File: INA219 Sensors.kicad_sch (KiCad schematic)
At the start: 20 parts, among them J5 Conn_01x06, U2 INA219AxD, U3 INA219AxD, U4 LTV-817, U5 LTV-817, U7 ESP32-C3 Pro Mini, U8 AMS1117-3.3

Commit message: DRC check
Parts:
- J5: value Conn_01x06 -> Esternal; footprint Connector_JST:JST_PH_S6B-PH-K_1x06_P2.00mm_Horizontal -> Connector_JST:JST_PH_B8B-PH-K_1x08_P2.00mm_Vertical; symbol Connector_Generic:Conn_01x06 -> Connector_Generic:Conn_01x08
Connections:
- net GNDPWR: no longer U8.4 (GND2)
- net at U7.0 (GPIO0/A0): now also J5.8 (Pin_8)
- net at U7.1 (GPIO1/A1): now also J5.7 (Pin_7)

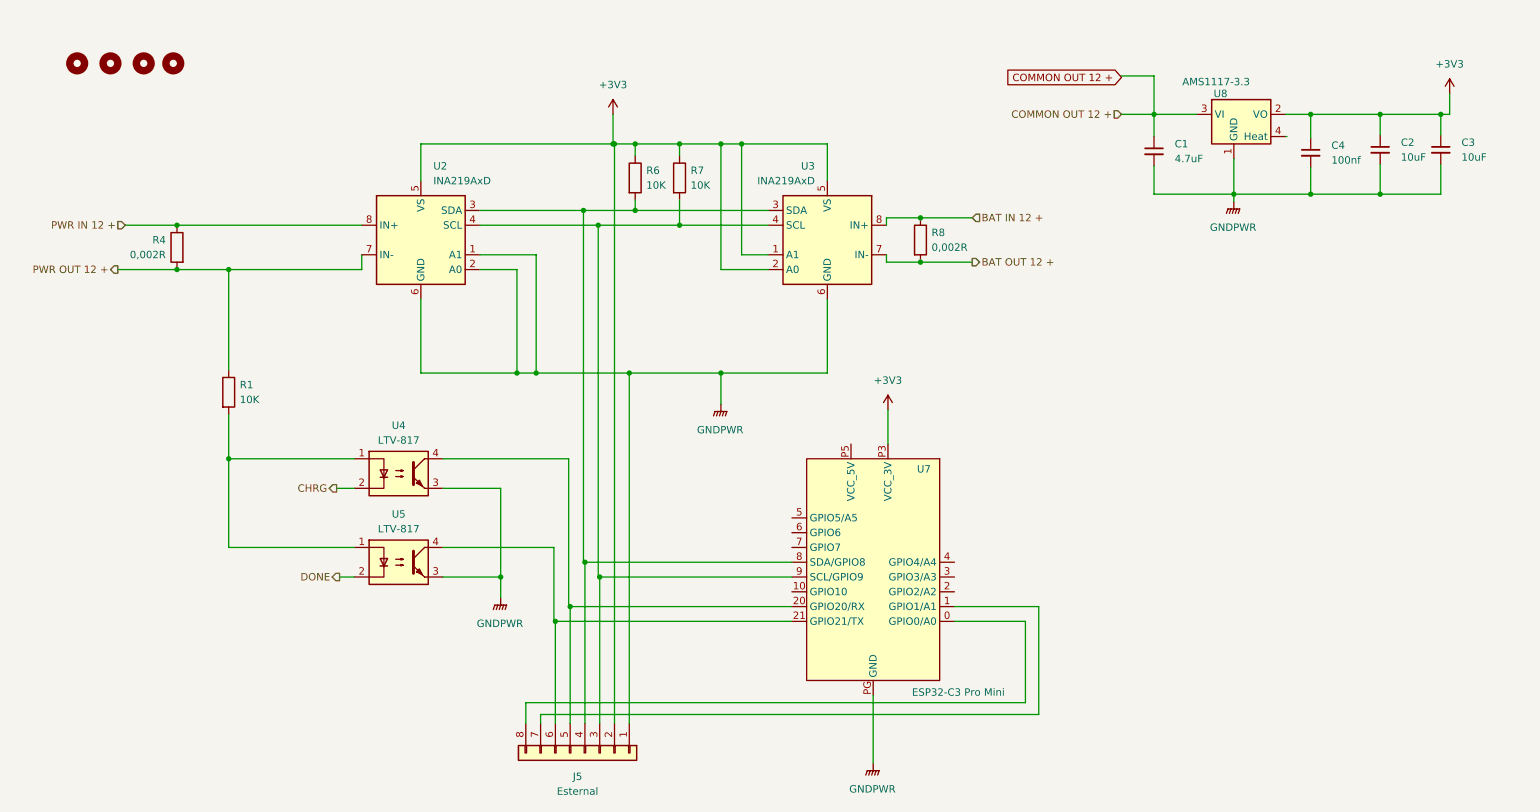
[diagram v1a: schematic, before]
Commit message: Add bat input stabilizer
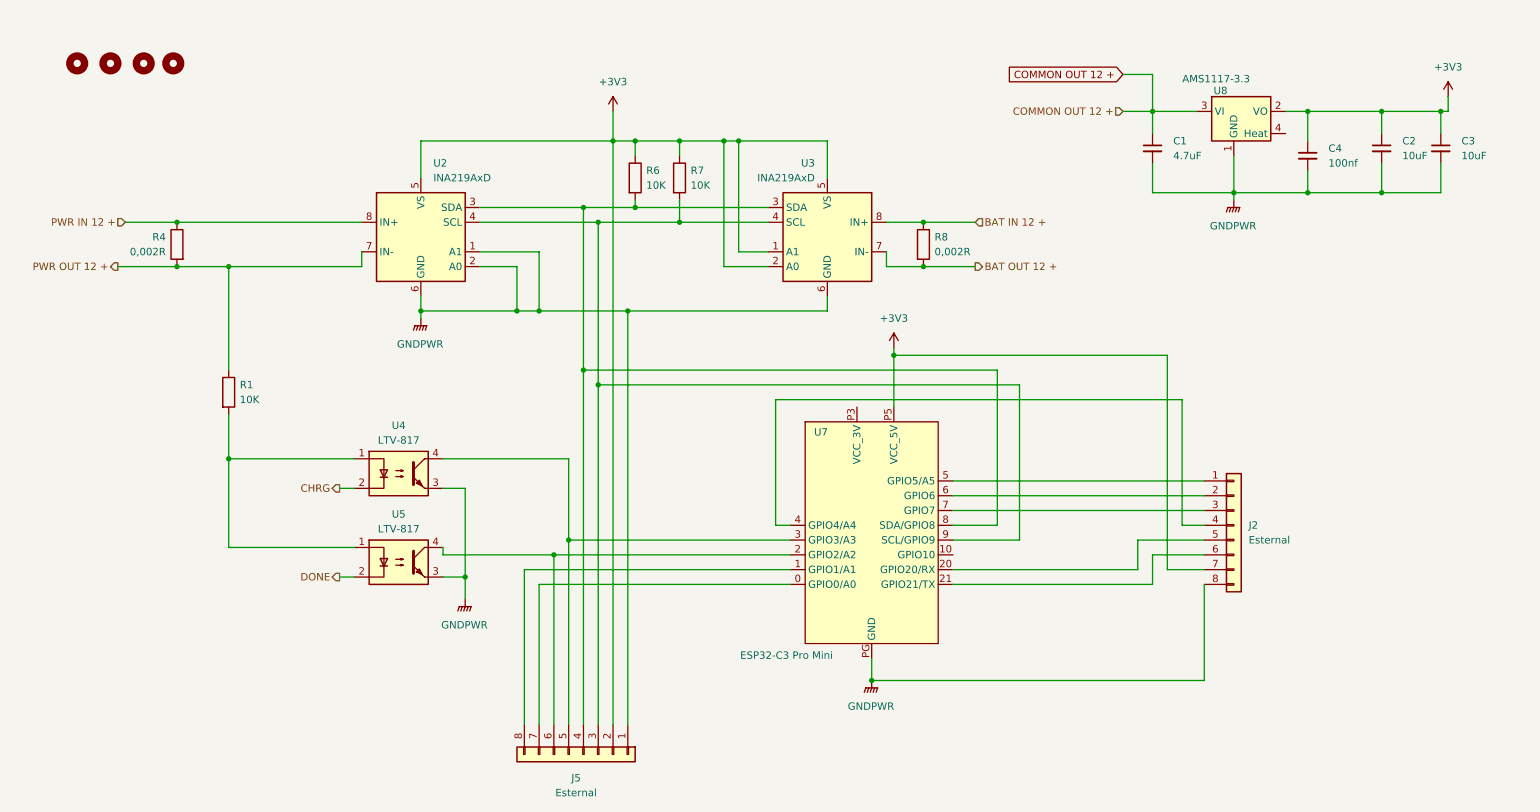
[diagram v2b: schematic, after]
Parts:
- added J2: Esternal, Connector_JST:JST_PH_B8B-PH-K_1x08_P2.00mm_Vertical, symbol Connector_Generic:Conn_01x08
- R1: footprint Resistor_SMD:R_0603_1608Metric_Pad0.98x0.95mm_HandSolder -> Resistor_SMD:R_0805_2012Metric_Pad1.20x1.40mm_HandSolder
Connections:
- net +3V3: now also U7.P5 (VCC_5V), J2.7 (Pin_7); no longer U7.P3 (VCC_3V)
- net GNDPWR: now also J2.8 (Pin_8)
- net at J5.5 (Pin_5), U4.4: now also U7.3 (GPIO3/A3); no longer U7.20 (GPIO20/RX)
- net at J5.6 (Pin_6), U5.4: now also U7.2 (GPIO2/A2); no longer U7.21 (GPIO21/TX)
- net at J5.7 (Pin_7): now also U7.0 (GPIO0/A0); no longer U7.1 (GPIO1/A1)
- net at J5.8 (Pin_8): now also U7.1 (GPIO1/A1); no longer U7.0 (GPIO0/A0)
- net at U7.4 (GPIO4/A4): now also J2.4 (Pin_4)
- net at U7.5 (GPIO5/A5): now also J2.1 (Pin_1)
- net at U7.6 (GPIO6): now also J2.2 (Pin_2)
- net at U7.7 (GPIO7): now also J2.3 (Pin_3)
- new net: J2.5 (Pin_5), U7.20 (GPIO20/RX)
- new net: J2.6 (Pin_6), U7.21 (GPIO21/TX)
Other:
- moved on the sheet: C1, C4, R4, R8, U2, U3, U7, U8

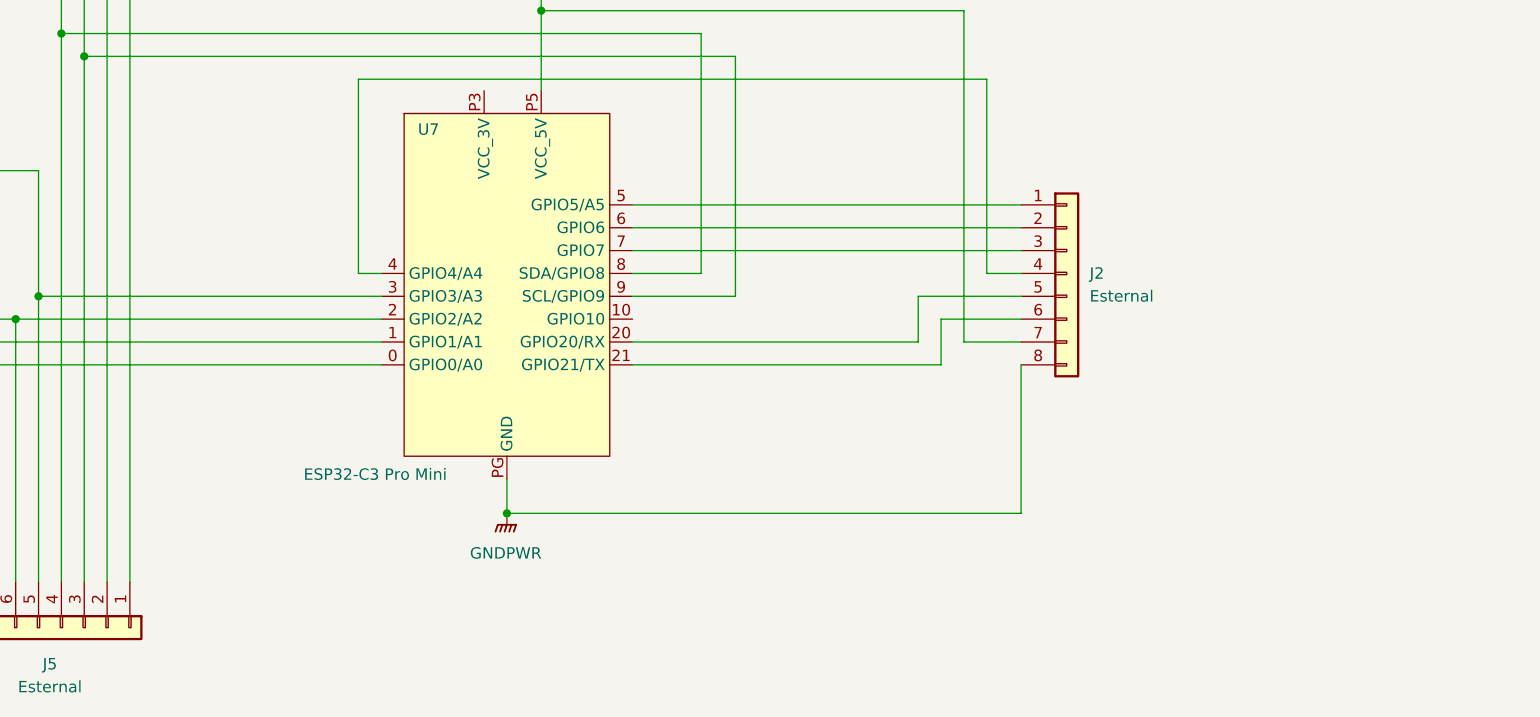
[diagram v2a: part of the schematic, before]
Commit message: Fix comparator out signal pullup
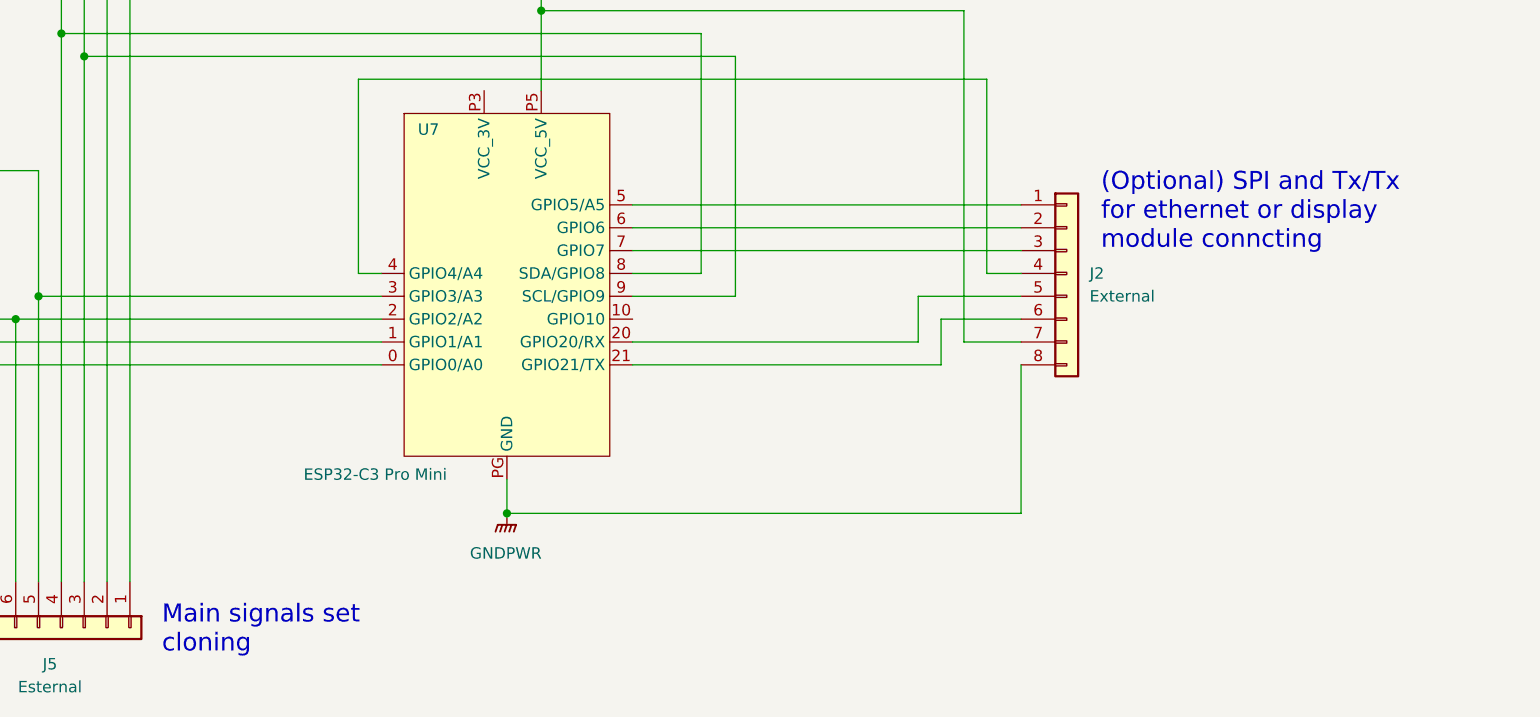
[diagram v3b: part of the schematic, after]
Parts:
- J2: value Esternal -> External
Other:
- note added: "(Optional) SPI and Tx/Tx for ethernet or display module conncting"
- note added: "Main signals set cloning"
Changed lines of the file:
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@@
 	(generator_version "9.0")
 	(paper "A4")
+	(text "Main signals set\ncloning "
+		(exclude_from_sim no)
+		(at 130.556 146.304 0)
+		(effects
+			(font
+				(size 2 2)
+			)
+			(justify left)
+		)
+	)
+	(text "(Optional) SPI and Tx/Tx \nfor ethernet or display\nmodule conncting"
+		(exclude_from_sim no)
+		(at 234.95 99.822 0)
+		(effects
+			(font
+				(size 2 2)
+			)
+			(justify left)
+		)
+	)
 	(junction
 		(at 128.27 52.07)
@@
 			)
 		)
-		(property "Value" "Esternal"
+		(property "Value" "External"
 			(at 233.68 109.2199 0)
 			(effects

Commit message: Add power sockwr
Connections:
- net at U4.4, U7.3 (GPIO3/A3): now also J5.8 (Pin_8); no longer J5.5 (Pin_5)
- net at U5.4, U7.2 (GPIO2/A2): now also J5.7 (Pin_7); no longer J5.6 (Pin_6)
- net at U7.0 (GPIO0/A0): now also J5.5 (Pin_5); no longer J5.7 (Pin_7)
- net at U7.1 (GPIO1/A1): now also J5.6 (Pin_6); no longer J5.8 (Pin_8)
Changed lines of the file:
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@@
-	)
-	(junction
-		(at 116.84 109.22)
-		(diameter 0)
-		(color 0 0 0 0)
 	)
 	(junction
@@
 	)
 	(junction
+		(at 109.22 109.22)
+		(diameter 0)
+		(color 0 0 0 0)
+	)
+	(junction
 		(at 121.92 54.61)
 		(diameter 0)
@@
 	)
 	(junction
-		(at 114.3 111.76)
-		(diameter 0)
-		(color 0 0 0 0)
-	)
-	(junction
 		(at 243.84 49.53)
 		(diameter 0)
@@
 	)
 	(junction
+		(at 111.76 111.76)
+		(diameter 0)
+		(color 0 0 0 0)
+	)
+	(junction
 		(at 58.42 62.23)
 		(diameter 0)
@@
 	(wire
 		(pts
-			(xy 154.94 114.3) (xy 109.22 114.3)
-		)
-		(stroke
-			(width 0)
-			(type default)
-		)
-	)
-	(wire
-		(pts
 			(xy 107.95 62.23) (xy 107.95 69.85)
 		)
@@
 	(wire
 		(pts
-			(xy 116.84 109.22) (xy 116.84 140.97)
-		)
-		(stroke
-			(width 0)
-			(type default)
-		)
-	)
-	(wire
-		(pts
 			(xy 222.25 106.68) (xy 226.06 106.68)
 		)
@@
 	(wire
 		(pts
+			(xy 111.76 111.76) (xy 154.94 111.76)
+		)
+		(stroke
+			(width 0)
+			(type default)
+		)
+	)
+	(wire
+		(pts
 			(xy 243.84 35.56) (xy 243.84 40.64)
 		)
@@
 	(wire
 		(pts
-			(xy 111.76 116.84) (xy 111.76 140.97)
-		)
-		(stroke
-			(width 0)
-			(type default)
-		)
-	)
-	(wire
-		(pts
 			(xy 231.14 43.18) (xy 231.14 49.53)
 		)
@@
 	(wire
 		(pts
-			(xy 109.22 114.3) (xy 109.22 140.97)
+			(xy 114.3 114.3) (xy 154.94 114.3)
 		)
 		(stroke
@@
 	(wire
 		(pts
-			(xy 114.3 111.76) (xy 154.94 111.76)
-		)
-		(stroke
-			(width 0)
-			(type default)
-		)
-	)
-	(wire
-		(pts
 			(xy 194.31 109.22) (xy 194.31 82.55)
 		)
@@
 	(wire
 		(pts
-			(xy 116.84 95.25) (xy 95.25 95.25)
+			(xy 109.22 95.25) (xy 95.25 95.25)
 		)
 		(stroke
@@
 	(wire
 		(pts
+			(xy 116.84 116.84) (xy 116.84 140.97)
+		)
+		(stroke
+			(width 0)
+			(type default)
+		)
+	)
+	(wire
+		(pts
 			(xy 212.09 35.56) (xy 217.17 35.56)
 		)
@@
 	(wire
 		(pts
+			(xy 116.84 116.84) (xy 154.94 116.84)
+		)
+		(stroke
+			(width 0)
+			(type default)
+		)
+	)
+	(wire
+		(pts
 			(xy 124.46 35.56) (xy 124.46 40.64)
 		)
@@
 	(wire
 		(pts
-			(xy 116.84 109.22) (xy 154.94 109.22)
+			(xy 109.22 109.22) (xy 154.94 109.22)
+		)
+		(stroke
+			(width 0)
+			(type default)
+		)
+	)
+	(wire
+		(pts
+			(xy 111.76 111.76) (xy 111.76 140.97)
 		)
 		(stroke
@@
 	(wire
 		(pts
-			(xy 114.3 111.76) (xy 114.3 140.97)
-		)
-		(stroke
-			(width 0)
-			(type default)
-		)
-	)
-	(wire
-		(pts
 			(xy 58.42 110.49) (xy 80.01 110.49)
 		)
@@
 	(wire
 		(pts
-			(xy 116.84 95.25) (xy 116.84 109.22)
-		)
-		(stroke
-			(width 0)
-			(type default)
-		)
-	)
-	(wire
-		(pts
-			(xy 154.94 116.84) (xy 111.76 116.84)
+			(xy 109.22 95.25) (xy 109.22 109.22)
 		)
 		(stroke
@@
 	(wire
 		(pts
+			(xy 114.3 114.3) (xy 114.3 140.97)
+		)
+		(stroke
+			(width 0)
+			(type default)
+		)
+	)
+	(wire
+		(pts
 			(xy 194.31 82.55) (xy 121.92 82.55)
 		)
@@
 	(wire
 		(pts
+			(xy 109.22 109.22) (xy 109.22 140.97)
+		)
+		(stroke
+			(width 0)
+			(type default)
+		)
+	)
+	(wire
+		(pts
 			(xy 91.44 69.85) (xy 91.44 71.12)
 		)
@@
 	(wire
 		(pts
-			(xy 114.3 111.76) (xy 95.25 111.76)
-		)
-		(stroke
+			(xy 95.25 111.76) (xy 111.76 111.76)
+		)
+		(stroke

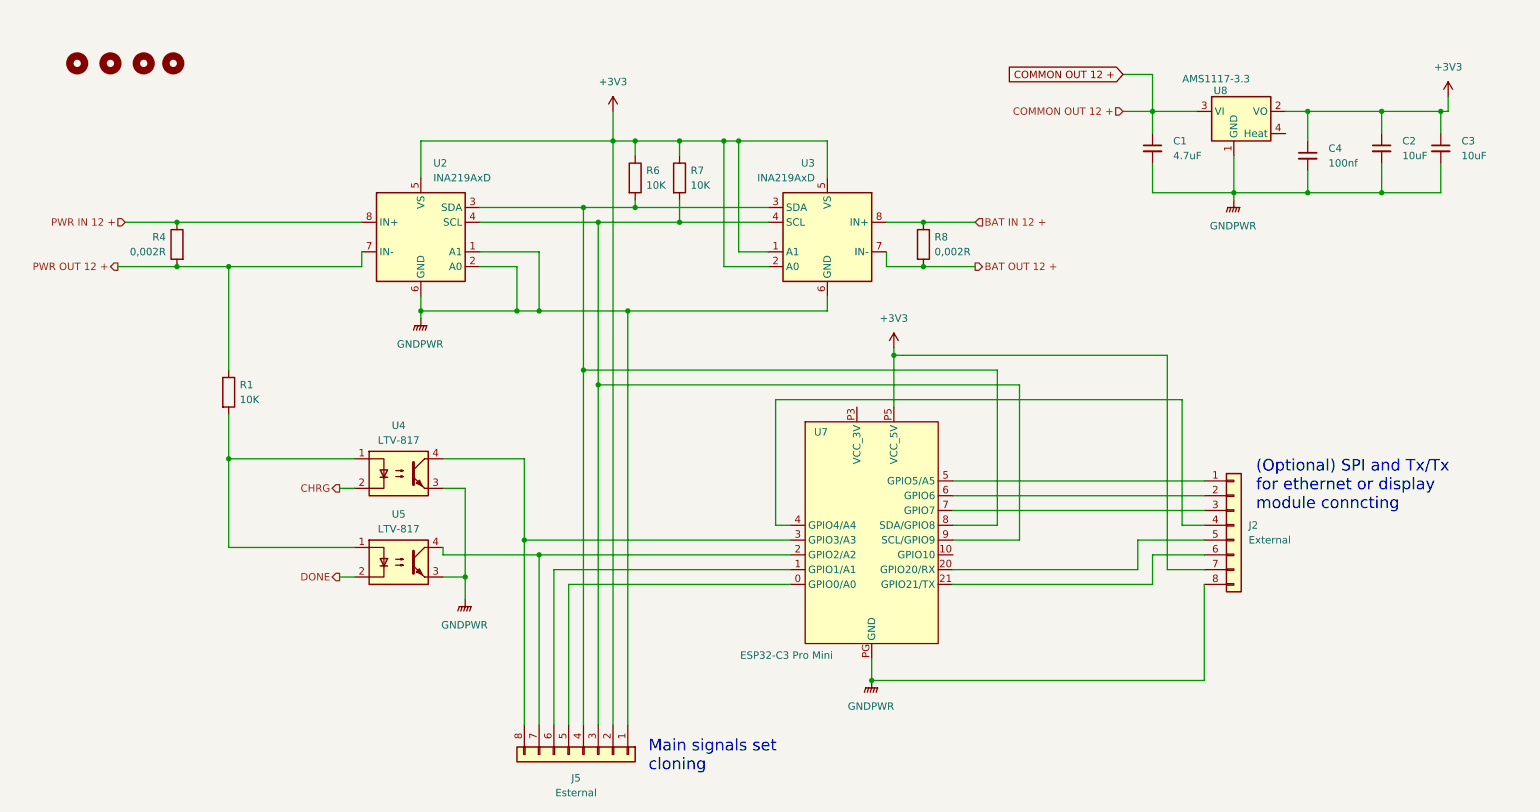
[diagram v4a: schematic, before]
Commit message: Clean space for second relay
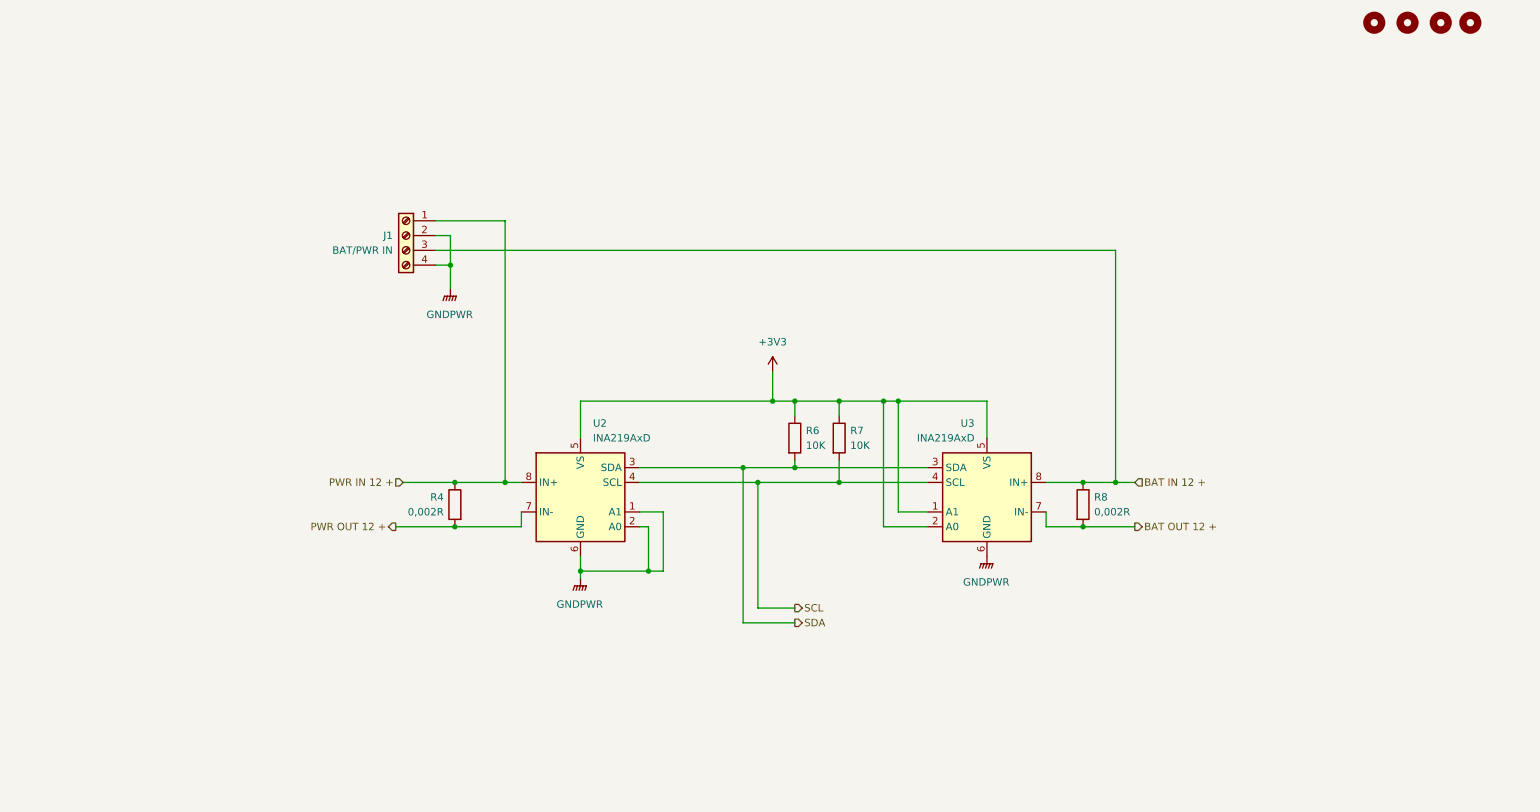
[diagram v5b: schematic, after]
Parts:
- removed C1: 4.7uF, Capacitor_SMD:C_1210_3225Metric_Pad1.33x2.70mm_HandSolder, symbol Device:C_Small
- removed C2, C3: 10uF, Capacitor_Tantalum_SMD:CP_EIA-3528-21_Kemet-B_HandSolder, symbol Device:C_Small
- removed C4: 100nf, Capacitor_SMD:C_0805_2012Metric_Pad1.18x1.45mm_HandSolder, symbol Device:C_Small
- removed J2: External, Connector_JST:JST_PH_B8B-PH-K_1x08_P2.00mm_Vertical, symbol Connector_Generic:Conn_01x08
- removed J5: Esternal, Connector_JST:JST_PH_B8B-PH-K_1x08_P2.00mm_Vertical, symbol Connector_Generic:Conn_01x08
- removed R1: 10K, Resistor_SMD:R_0805_2012Metric_Pad1.20x1.40mm_HandSolder, symbol Device:R
- removed U4, U5: LTV-817, Package_DIP:DIP-4_W7.62mm, symbol Isolator:LTV-817
- removed U7: ESP32-C3 Pro Mini, WIFI_Module:ESP32-C3_Pro_mini_pin, symbol MCU_Module_local:ESP32_C3_Pro_Mini
- removed U8: AMS1117-3.3, Package_TO_SOT_SMD:SOT-223-3_TabPin2, symbol Regulator_Linear:AMS1117-3.3
- added J1: BAT/PWR IN, TerminalBlock_Local:ScrewTerminal_KF7.62_4P, symbol Connector:Screw_Terminal_01x04
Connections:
- net BAT IN 12 +: now also J1.3 (Pin_3)
- net GNDPWR: now also J1.2 (Pin_2), J1.4 (Pin_4)
- net PWR IN 12 +: now also J1.1 (Pin_1)
- net SDA: now reaches R6.2, U2.3 (SDA), U3.3 (SDA)
- net SCL: now reaches R7.2, U2.4 (SCL), U3.4 (SCL)
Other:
- note removed: "(Optional) SPI and Tx/Tx for ethernet or display module conncting"
- note removed: "Main signals set cloning"
- moved on the sheet: R4, R6, R7, R8, U2, U3
